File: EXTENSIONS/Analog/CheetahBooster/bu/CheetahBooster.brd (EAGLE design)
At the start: 83 x 73 mm, 28 parts

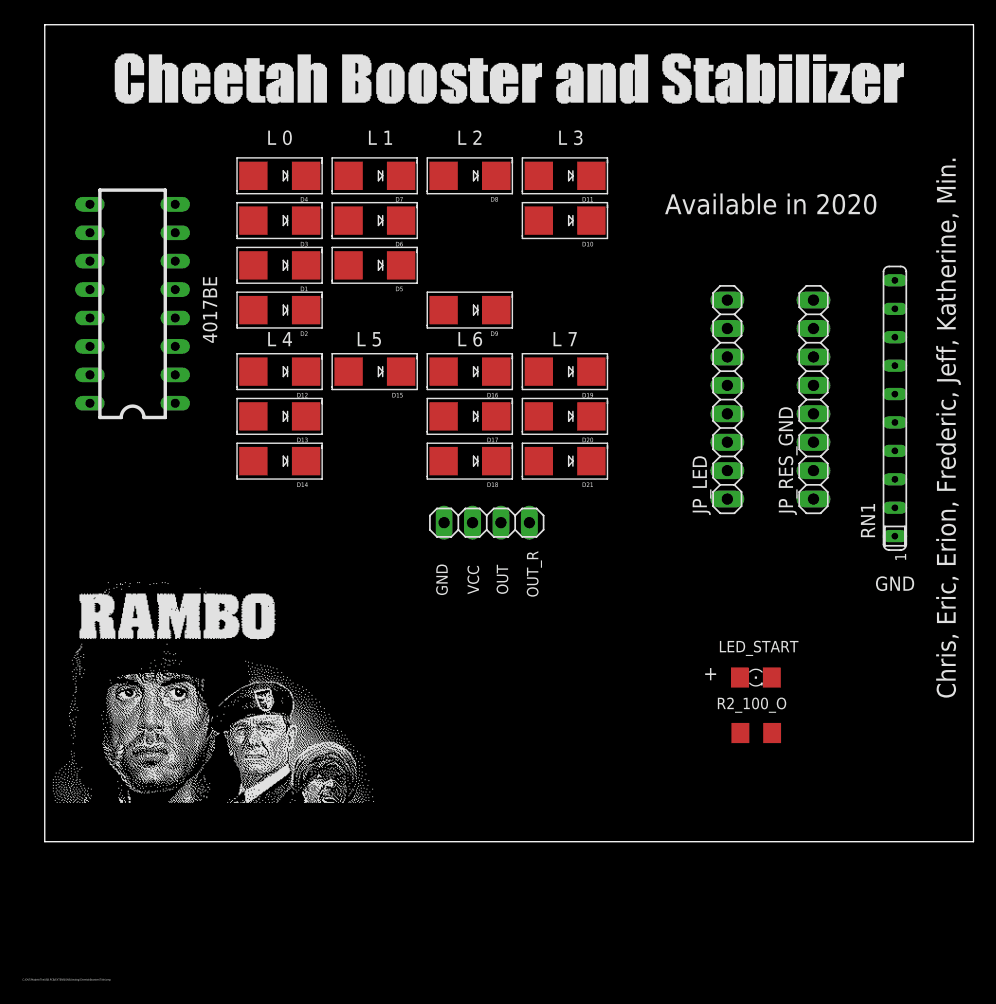
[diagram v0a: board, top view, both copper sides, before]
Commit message: Create CheetahBooster MCU
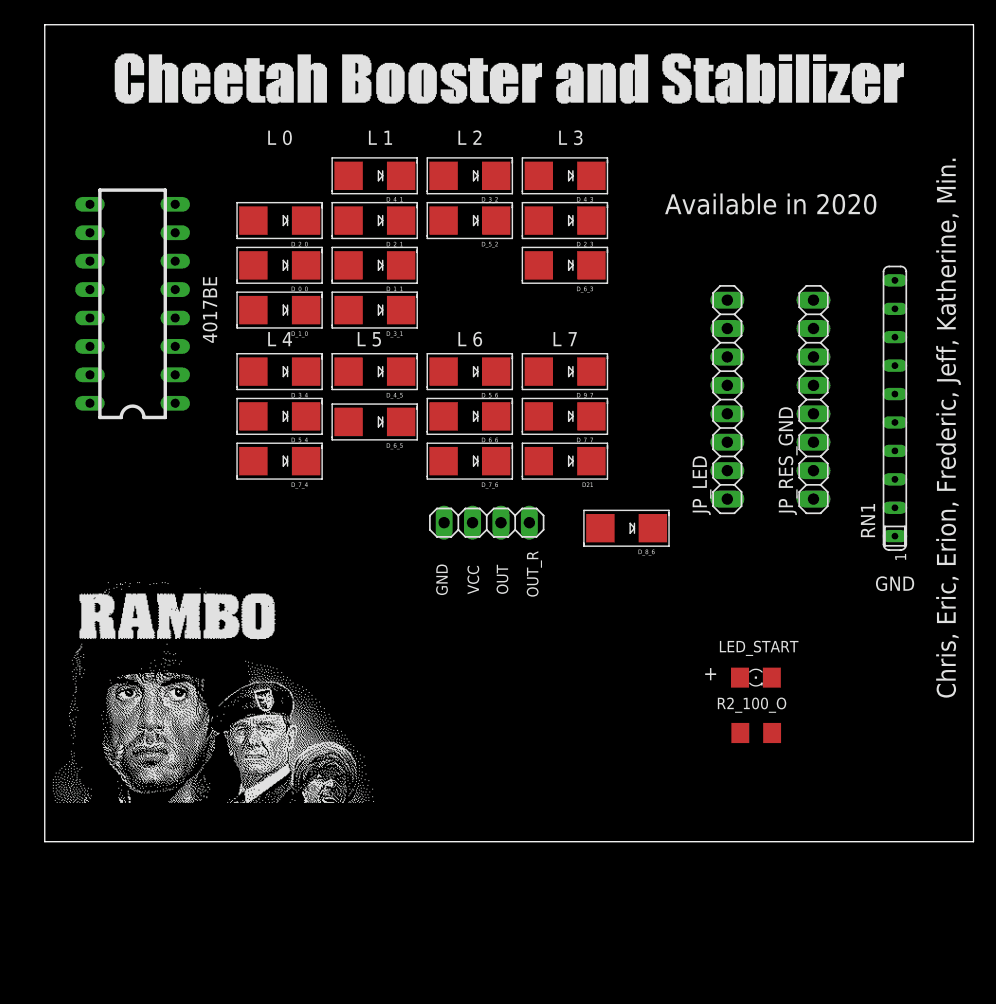
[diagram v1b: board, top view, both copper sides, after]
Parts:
- removed D4, D9: (no value), adafruit:SMADIODE
- added D_3_1, D_5_2, D_6_3, D_6_5, D_8_6: (no value), adafruit:SMADIODE
- renumbered D1 to D_0_0, D10 to D_2_3, D11 to D_4_3, D12 to D_3_4, D13 to D_5_4, D14 to D_7_4, D15 to D_4_5, D16 to D_5_6, D17 to D_6_6, D18 to D_7_6, D19 to D_9_7, D2 to D_1_0, D20 to D_7_7, D3 to D_2_0, D5 to D_1_1, D6 to D_2_1, D7 to D_4_1, D8 to D_3_2
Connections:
- new net D_8_7: D21.C
- new net SEG_9: 4017BE.11, D_9_7.A
- net LED_0: no longer D4.C
- net LED_1: now also D_3_1.C
- net LED_2: now also D_5_2.C; no longer D9.C
- net LED_3: now also D_6_3.C
- net LED_5: now also D_6_5.C
- net LED_6: now also D_8_6.C
- net LED_7: no longer D21.C
- net RESET: no longer 4017BE.11
- net SEG_3: now also D_3_1.A; no longer D4.A
- net SEG_5: now also D_5_2.A; no longer D9.A
- net SEG_6: now also D_6_3.A, D_6_5.A; no longer D_7_4.A, D_9_7.A
- net SEG_7: now also D_7_4.A
- net SEG_8: now also D_8_6.A
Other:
- board text removed: "C:/DVT/MadeInTheUSB.PCB/EXTENSIONS/Analog/CheetahBooster/Title.bmp"

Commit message: Create CheetahBooster MCU
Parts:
- moved D_2_3 4.00 mm to (52.5, 67.5)
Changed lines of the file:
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@@
 <element name="D_3_2" library="adafruit" package="SMADIODE" value="" x="40" y="71.5" rot="R180"/>
 <element name="D_5_2" library="adafruit" package="SMADIODE" value="" x="40" y="67.5" rot="R180"/>
-<element name="D_2_3" library="adafruit" package="SMADIODE" value="" x="48.5" y="67.5" rot="R180"/>
+<element name="D_2_3" library="adafruit" package="SMADIODE" value="" x="52.5" y="67.5" rot="R180"/>
 <element name="D_4_3" library="adafruit" package="SMADIODE" value="" x="48.5" y="71.5" rot="R180"/>
 <element name="D_3_4" library="adafruit" package="SMADIODE" value="" x="23" y="54" rot="R180"/>
@@
 <contactref element="D_2_1" pad="A"/>
 <contactref element="D_2_3" pad="A"/>
-<wire x1="29.1505" y1="67.5" x2="46.1505" y2="67.5" width="0" layer="19" extent="1-1"/>
+<wire x1="29.1505" y1="67.5" x2="50.1505" y2="67.5" width="0" layer="19" extent="1-1"/>
 <wire x1="20.6505" y1="67.5" x2="29.1505" y2="67.5" width="0" layer="19" extent="1-1"/>
 <wire x1="13.658965625" y1="58.790809375" x2="20.6505" y2="67.5" width="0" layer="19" extent="1-1"/>
@@
 <contactref element="D_6_3" pad="C"/>
 <contactref element="D_2_3" pad="C"/>
-<wire x1="50.8495" y1="67.5" x2="50.8495" y2="71.5" width="0" layer="19" extent="1-1"/>
-<wire x1="50.8495" y1="63.5" x2="50.8495" y2="67.5" width="0" layer="19" extent="1-1"/>
+<wire x1="54.8495" y1="67.5" x2="50.8495" y2="71.5" width="0" layer="19" extent="1-1"/>
+<wire x1="50.8495" y1="63.5" x2="54.8495" y2="67.5" width="0" layer="19" extent="1-1"/>
 <wire x1="63" y1="50.23" x2="50.8495" y2="63.5" width="0" layer="19" extent="1-1"/>
 </signal>
